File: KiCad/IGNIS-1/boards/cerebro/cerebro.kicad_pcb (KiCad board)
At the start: 2 copper layers, 62 x 62 mm, 22 parts, among them J1 LiPo_1S_in, J2 RBF_pin, J40 Backplane_2x10, Q1 MMBT3904, SW1 Main_SW, U10 ESP32-WROOM-32E DevKit 40p, U2 TPS63020

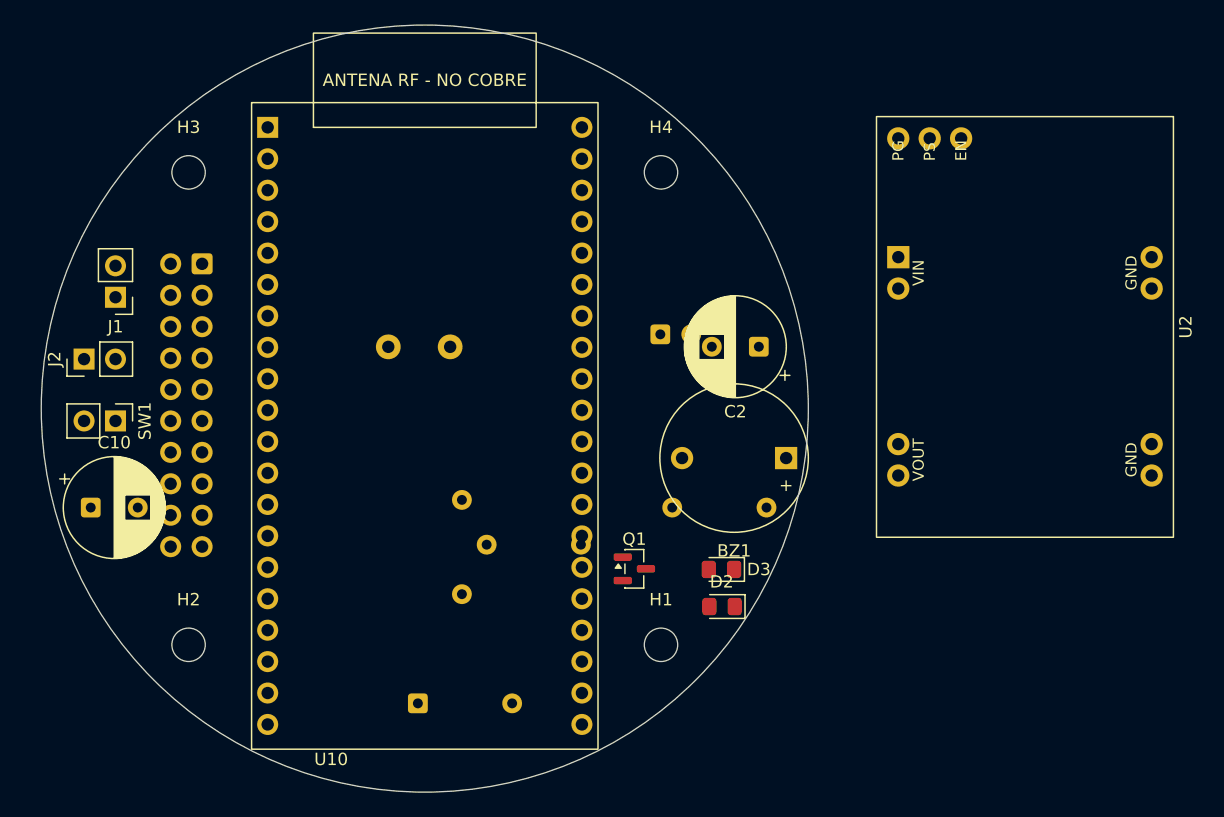
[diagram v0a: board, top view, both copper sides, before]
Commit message: Energia: split en 2 boards (carga + energia) y redistribucion de rieles
- Board carga (5º): TP4056 + bateria + RBF + SW1 + TPS63020 -> +3V3 y VSW al bus
- Board energia (4º): MT3608 -> +5V al bus (toma VSW)
- Simbolos nuevos: TP4056, TPS63020; footprints TP4056_HW373, SW_Slide_SS12D00
- Bus: +3V3(p1), +5V(p19), VSW(p20), GND(2/4/11); backplane a header plano
- cerebro: quitada seccion de energia duplicada (U2/J1/J2/SW1/C1), +3V3 del bus
- sensores: quitado MT3608 (U3), +5V del bus alimenta MQ-135/GPS
- ZC323200 eliminado (sin uso)

Co-Authored-By: Claude Opus 4.8 <noreply@anthropic.com>
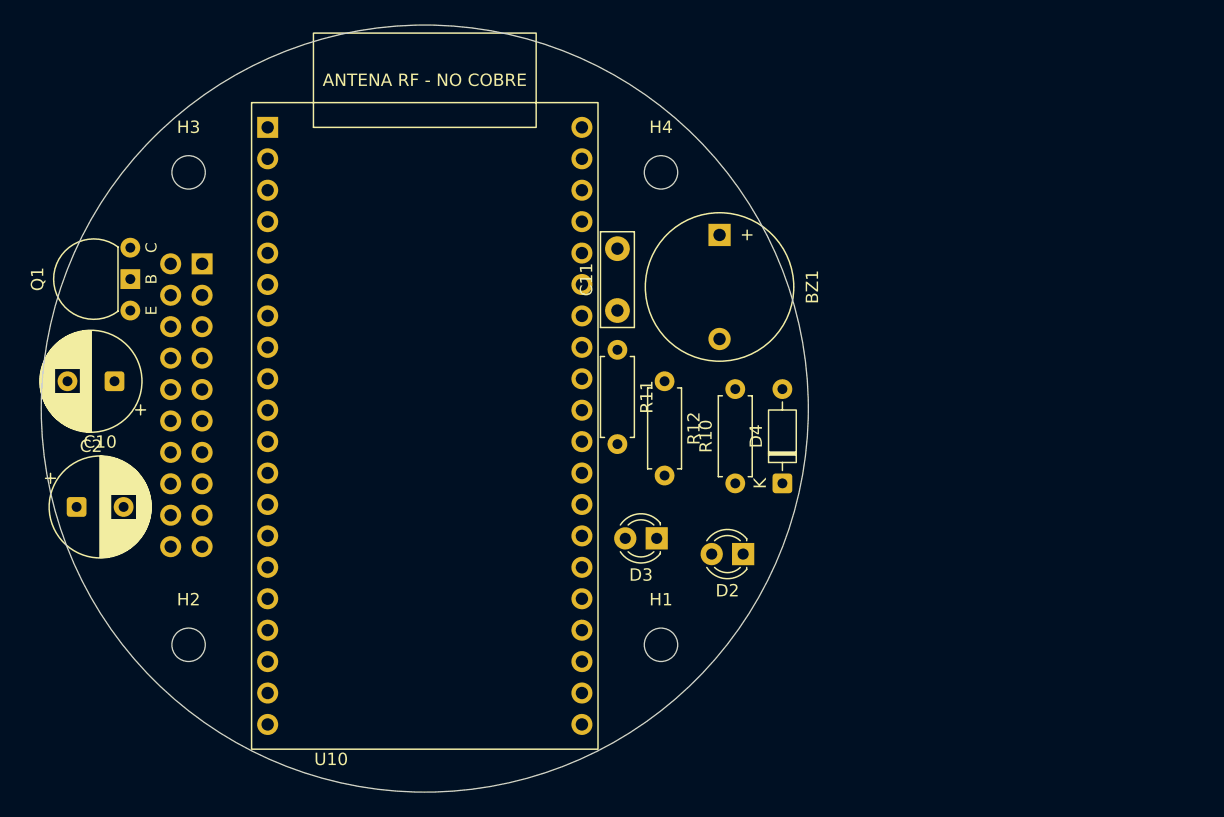
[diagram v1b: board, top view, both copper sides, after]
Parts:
- removed C1: 22uF, Capacitor_THT:CP_Radial_D6.3mm_P2.50mm
- removed J1: LiPo_1S_in, Connector_PinHeader_2.54mm:PinHeader_1x02_P2.54mm_Vertical
- removed J2: RBF_pin, Connector_PinHeader_2.54mm:PinHeader_1x02_P2.54mm_Vertical
- removed SW1: Main_SW, Connector_PinHeader_2.54mm:PinHeader_1x02_P2.54mm_Vertical
- removed U2: TPS63020, IGNIS1:TPS63020_module
- C11, D4, R10, R11, R12: moved to F.Cu
- D2, D3: footprint LED_SMD:LED_0805_2012Metric_Pad1.15x1.40mm_HandSolder -> LED_THT:LED_D3.0mm
- J40: footprint Connector_IDC:IDC-Header_2x10_P2.54mm_Vertical -> Connector_PinHeader_2.54mm:PinHeader_2x10_P2.54mm_Vertical
- Q1: footprint Package_TO_SOT_SMD:SOT-23 -> IGNIS1:Q_TO92_2N3904_EBC
- moved C2 52.2 mm to (74.9, 97.8)
- moved Q1 47.0 mm to (76.2, 89.5), turned to 90 degrees
- moved D4 34.4 mm to (128.9, 106.0), turned to 90 degrees
- moved R10 23.8 mm to (125.1, 106.0)
- moved R12 19.5 mm to (119.4, 97.8), turned to -90 degrees
- moved BZ1 13.9 mm to (123.8, 90.2), turned to -90 degrees
- moved C11 13.8 mm to (115.6, 92.1), turned to 90 degrees
- moved R11 13.5 mm to (115.6, 95.2), turned to -90 degrees
- moved D3 5.80 mm to (118.7, 110.5)
- moved D2 4.57 mm to (125.7, 111.8)
- moved C10 1.14 mm to (71.9, 108.0)
